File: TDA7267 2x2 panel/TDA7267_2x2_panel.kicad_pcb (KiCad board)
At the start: 2 copper layers, 89 x 81 mm, 72 parts, among them U1 TDA7267

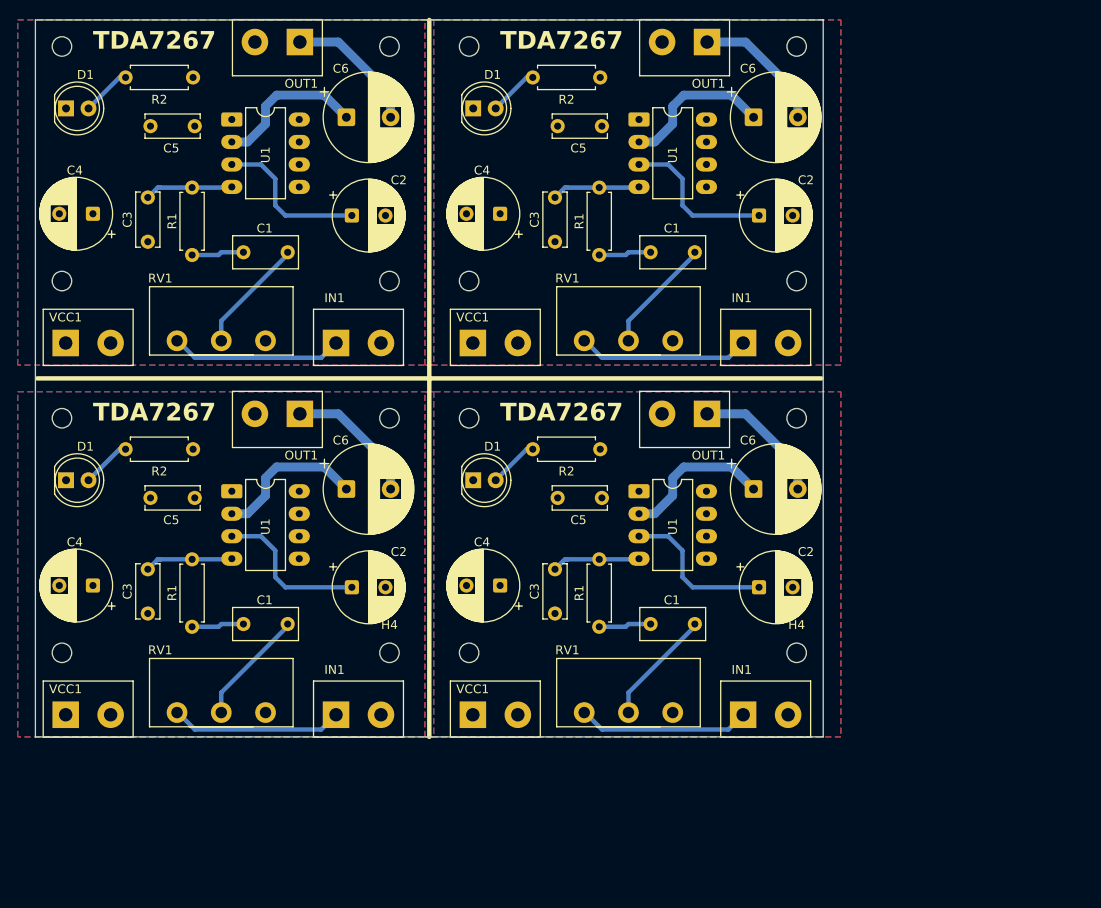
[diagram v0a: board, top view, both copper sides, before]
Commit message: Bottom GND plane
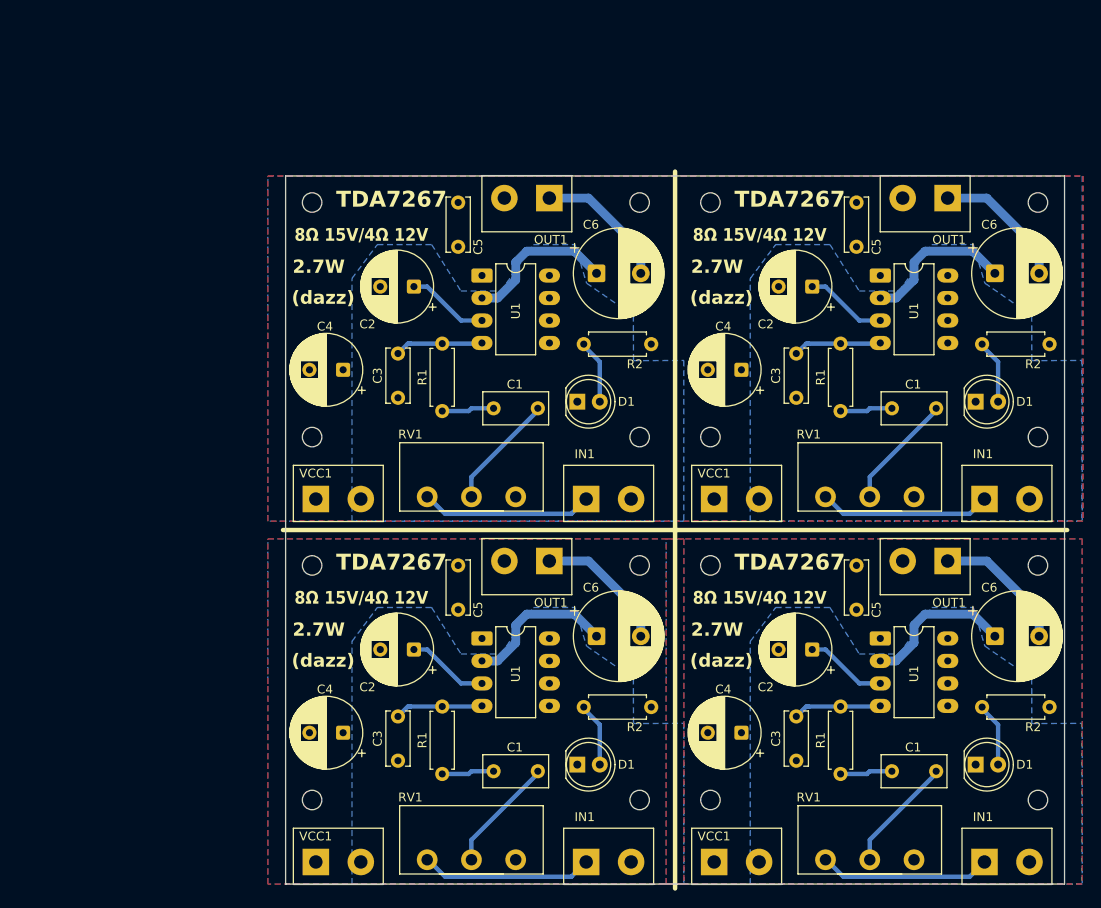
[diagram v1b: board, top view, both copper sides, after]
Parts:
- removed the C1 at (146.5, 97.2)
- removed the C1 at (100.5, 97.2)
- removed the C1 at (100.5, 55.2)
- removed the C1 at (146.5, 55.2)
- removed the C2 at (107.8, 51.1)
- removed the C2 at (153.8, 93.1)
- removed the C2 at (153.8, 51.1)
- removed the C2 at (107.8, 93.1)
- removed the C3 at (130.7, 54.1)
- removed the C3 at (84.7, 96.1)
- removed the C3 at (84.7, 54.1)
- removed the C3 at (130.7, 96.1)
- removed the C4 at (78.5, 92.9)
- removed the C4 at (124.5, 50.9)
- removed the C4 at (78.5, 50.9)
- removed the C4 at (124.5, 92.9)
- removed the C5 at (131.0, 41.0)
- removed the C5 at (131.0, 83.0)
- removed the C5 at (85.0, 41.0)
- removed the C5 at (85.0, 83.0)
- removed the C6 at (107.1, 40.0)
- removed the C6 at (107.1, 82.0)
- removed the C6 at (153.1, 82.0)
- removed the C6 at (153.1, 40.0)
- removed the D1 at (121.5, 39.0)
- removed the D1 at (75.5, 81.0)
- removed the D1 at (75.5, 39.0)
- removed the D1 at (121.5, 81.0)
- removed the H1 at (75.0, 74.0)
- removed the H1 at (75.0, 32.0)
- removed the H1 at (121.0, 32.0)
- removed the H1 at (121.0, 74.0)
- removed the H2 at (158.0, 74.0)
- removed the H2 at (112.0, 32.0)
- removed the H2 at (158.0, 32.0)
- removed the H2 at (112.0, 74.0)
- removed the H3 at (121.0, 100.5)
- removed the H3 at (121.0, 58.5)
- removed the H3 at (75.0, 58.5)
- removed the H3 at (75.0, 100.5)
- removed the H4 at (112.0, 58.5)
- removed the H4 at (158.0, 100.5)
- removed the H4 at (158.0, 58.5)
- removed the H4 at (112.0, 100.5)
- removed the IN1 at (152.0, 107.5)
- removed the IN1 at (106.0, 107.5)
- removed the IN1 at (106.0, 65.5)
- removed the IN1 at (152.0, 65.5)
- removed the OUT1 at (101.9, 73.5)
- removed the OUT1 at (147.9, 73.5)
- removed the OUT1 at (101.9, 31.5)
- removed the OUT1 at (147.9, 31.5)
- removed the R1 at (89.7, 55.6)
- removed the R1 at (135.7, 55.6)
- removed the R1 at (89.7, 97.6)
- removed the R1 at (135.7, 97.6)
- removed the R2 at (128.2, 77.5)
- removed the R2 at (128.2, 35.5)
- removed the R2 at (82.2, 35.5)
- removed the R2 at (82.2, 77.5)
- removed the RV1 at (88.0, 107.2)
- removed the RV1 at (134.0, 65.2)
- removed the RV1 at (134.0, 107.2)
- removed the RV1 at (88.0, 65.2)
- removed the U1 at (94.2, 40.2)
- removed the U1 at (140.2, 40.2)
- removed the U1 at (94.2, 82.2)
- removed the U1 at (140.2, 82.2)
- removed the VCC1 at (75.4, 65.5)
- removed the VCC1 at (121.4, 107.5)
- removed the VCC1 at (75.4, 107.5)
- removed the VCC1 at (121.4, 65.5)
- added C1: 1uF, Capacitor_THT:C_Rect_L7.2mm_W3.5mm_P5.00mm_FKS2_FKP2_MKS2_MKP2, F.Cu at (128.8, 72.9)
- added C1: 1uF, Capacitor_THT:C_Rect_L7.2mm_W3.5mm_P5.00mm_FKS2_FKP2_MKS2_MKP2, F.Cu at (173.8, 113.9)
- added C1: 1uF, Capacitor_THT:C_Rect_L7.2mm_W3.5mm_P5.00mm_FKS2_FKP2_MKS2_MKP2, F.Cu at (173.8, 72.9)
- added C1: 1uF, Capacitor_THT:C_Rect_L7.2mm_W3.5mm_P5.00mm_FKS2_FKP2_MKS2_MKP2, F.Cu at (128.8, 113.9)
- added C2: 47uF, Capacitor_THT:CP_Radial_D8.0mm_P3.80mm, F.Cu at (114.8, 100.1)
- added C2: 47uF, Capacitor_THT:CP_Radial_D8.0mm_P3.80mm, F.Cu at (159.8, 100.1)
- added C2: 47uF, Capacitor_THT:CP_Radial_D8.0mm_P3.80mm, F.Cu at (114.8, 59.1)
- added C2: 47uF, Capacitor_THT:CP_Radial_D8.0mm_P3.80mm, F.Cu at (159.8, 59.1)
- added C3: 470pF, Capacitor_THT:C_Disc_D6.0mm_W2.5mm_P5.00mm, F.Cu at (113.0, 112.7)
- added C3: 470pF, Capacitor_THT:C_Disc_D6.0mm_W2.5mm_P5.00mm, F.Cu at (113.0, 71.7)
- added C3: 470pF, Capacitor_THT:C_Disc_D6.0mm_W2.5mm_P5.00mm, F.Cu at (158.0, 71.7)
- added C3: 470pF, Capacitor_THT:C_Disc_D6.0mm_W2.5mm_P5.00mm, F.Cu at (158.0, 112.7)
- added C4: 100uF, Capacitor_THT:CP_Radial_D8.0mm_P3.80mm, F.Cu at (151.8, 109.5)
- added C4: 100uF, Capacitor_THT:CP_Radial_D8.0mm_P3.80mm, F.Cu at (106.8, 68.5)
- added C4: 100uF, Capacitor_THT:CP_Radial_D8.0mm_P3.80mm, F.Cu at (151.8, 68.5)
- added C4: 100uF, Capacitor_THT:CP_Radial_D8.0mm_P3.80mm, F.Cu at (106.8, 109.5)
- added C5: 100nF, Capacitor_THT:C_Disc_D6.0mm_W2.5mm_P5.00mm, F.Cu at (164.8, 90.6)
- added C5: 100nF, Capacitor_THT:C_Disc_D6.0mm_W2.5mm_P5.00mm, F.Cu at (119.8, 90.6)
- added C5: 100nF, Capacitor_THT:C_Disc_D6.0mm_W2.5mm_P5.00mm, F.Cu at (164.8, 49.6)
- added C5: 100nF, Capacitor_THT:C_Disc_D6.0mm_W2.5mm_P5.00mm, F.Cu at (119.8, 49.6)
- added C6: 1000uF, Capacitor_THT:CP_Radial_D10.0mm_P5.00mm, F.Cu at (180.4, 98.6)
- added C6: 1000uF, Capacitor_THT:CP_Radial_D10.0mm_P5.00mm, F.Cu at (180.4, 57.6)
- added C6: 1000uF, Capacitor_THT:CP_Radial_D10.0mm_P5.00mm, F.Cu at (135.4, 98.6)
- added C6: 1000uF, Capacitor_THT:CP_Radial_D10.0mm_P5.00mm, F.Cu at (135.4, 57.6)
- added D1: LED, LED_THT:LED_D5.0mm, F.Cu at (133.2, 113.1)
- added D1: LED, LED_THT:LED_D5.0mm, F.Cu at (178.2, 72.1)
- added D1: LED, LED_THT:LED_D5.0mm, F.Cu at (133.2, 72.1)
- added D1: LED, LED_THT:LED_D5.0mm, F.Cu at (178.2, 113.1)
- added H1: MountingHole, MountingHole:MountingHole_2.2mm_M2, F.Cu at (148.3, 90.6)
- added H1: MountingHole, MountingHole:MountingHole_2.2mm_M2, F.Cu at (148.3, 49.6)
- added H1: MountingHole, MountingHole:MountingHole_2.2mm_M2, F.Cu at (103.3, 49.6)
- added H1: MountingHole, MountingHole:MountingHole_2.2mm_M2, F.Cu at (103.3, 90.6)
- added H2: MountingHole, MountingHole:MountingHole_2.2mm_M2, F.Cu at (185.3, 49.6)
- added H2: MountingHole, MountingHole:MountingHole_2.2mm_M2, F.Cu at (140.3, 49.6)
- added H2: MountingHole, MountingHole:MountingHole_2.2mm_M2, F.Cu at (140.3, 90.6)
- added H2: MountingHole, MountingHole:MountingHole_2.2mm_M2, F.Cu at (185.3, 90.6)
- added H3: MountingHole, MountingHole:MountingHole_2.2mm_M2, F.Cu at (103.3, 76.1)
- added H3: MountingHole, MountingHole:MountingHole_2.2mm_M2, F.Cu at (148.3, 117.1)
- added H3: MountingHole, MountingHole:MountingHole_2.2mm_M2, F.Cu at (103.3, 117.1)
- added H3: MountingHole, MountingHole:MountingHole_2.2mm_M2, F.Cu at (148.3, 76.1)
- added H4: MountingHole, MountingHole:MountingHole_2.2mm_M2, F.Cu at (140.3, 76.1)
- added H4: MountingHole, MountingHole:MountingHole_2.2mm_M2, F.Cu at (185.3, 117.1)
- added H4: MountingHole, MountingHole:MountingHole_2.2mm_M2, F.Cu at (140.3, 117.1)
- added H4: MountingHole, MountingHole:MountingHole_2.2mm_M2, F.Cu at (185.3, 76.1)
- added IN1: Conn_01x02_Pin, TerminalBlock:TerminalBlock_bornier-2_P5.08mm, F.Cu at (134.2, 124.1)
- added IN1: Conn_01x02_Pin, TerminalBlock:TerminalBlock_bornier-2_P5.08mm, F.Cu at (179.2, 83.1)
- added IN1: Conn_01x02_Pin, TerminalBlock:TerminalBlock_bornier-2_P5.08mm, F.Cu at (134.2, 83.1)
- added IN1: Conn_01x02_Pin, TerminalBlock:TerminalBlock_bornier-2_P5.08mm, F.Cu at (179.2, 124.1)
- added OUT1: Conn_01x02_Pin, TerminalBlock:TerminalBlock_bornier-2_P5.08mm, F.Cu at (130.1, 90.1)
- added OUT1: Conn_01x02_Pin, TerminalBlock:TerminalBlock_bornier-2_P5.08mm, F.Cu at (175.1, 49.1)
- added OUT1: Conn_01x02_Pin, TerminalBlock:TerminalBlock_bornier-2_P5.08mm, F.Cu at (130.1, 49.1)
- added OUT1: Conn_01x02_Pin, TerminalBlock:TerminalBlock_bornier-2_P5.08mm, F.Cu at (175.1, 90.1)
- added R1: 1K, Resistor_THT:R_Axial_DIN0207_L6.3mm_D2.5mm_P7.62mm_Horizontal, F.Cu at (118.0, 73.2)
- added R1: 1K, Resistor_THT:R_Axial_DIN0207_L6.3mm_D2.5mm_P7.62mm_Horizontal, F.Cu at (163.0, 73.2)
- added R1: 1K, Resistor_THT:R_Axial_DIN0207_L6.3mm_D2.5mm_P7.62mm_Horizontal, F.Cu at (118.0, 114.2)
- added R1: 1K, Resistor_THT:R_Axial_DIN0207_L6.3mm_D2.5mm_P7.62mm_Horizontal, F.Cu at (163.0, 114.2)
- added R2: 1K, Resistor_THT:R_Axial_DIN0207_L6.3mm_D2.5mm_P7.62mm_Horizontal, F.Cu at (179.0, 65.6)
- added R2: 1K, Resistor_THT:R_Axial_DIN0207_L6.3mm_D2.5mm_P7.62mm_Horizontal, F.Cu at (179.0, 106.6)
- added R2: 1K, Resistor_THT:R_Axial_DIN0207_L6.3mm_D2.5mm_P7.62mm_Horizontal, F.Cu at (134.0, 65.6)
- added R2: 1K, Resistor_THT:R_Axial_DIN0207_L6.3mm_D2.5mm_P7.62mm_Horizontal, F.Cu at (134.0, 106.6)
- added RV1: A10K, Potentiometer_THT:Potentiometer_Piher_T-16H_Single_Horizontal, F.Cu at (116.3, 82.9)
- added RV1: A10K, Potentiometer_THT:Potentiometer_Piher_T-16H_Single_Horizontal, F.Cu at (161.3, 123.9)
- added RV1: A10K, Potentiometer_THT:Potentiometer_Piher_T-16H_Single_Horizontal, F.Cu at (116.3, 123.9)
- added RV1: A10K, Potentiometer_THT:Potentiometer_Piher_T-16H_Single_Horizontal, F.Cu at (161.3, 82.9)
- added U1: TDA7267, Package_DIP:DIP-8_W7.62mm_LongPads, F.Cu at (167.5, 57.9)
- added U1: TDA7267, Package_DIP:DIP-8_W7.62mm_LongPads, F.Cu at (122.5, 57.9)
- added U1: TDA7267, Package_DIP:DIP-8_W7.62mm_LongPads, F.Cu at (122.5, 98.9)
- added U1: TDA7267, Package_DIP:DIP-8_W7.62mm_LongPads, F.Cu at (167.5, 98.9)
- added VCC1: Conn_01x02_Pin, TerminalBlock:TerminalBlock_bornier-2_P5.08mm, F.Cu at (148.7, 83.1)
- added VCC1: Conn_01x02_Pin, TerminalBlock:TerminalBlock_bornier-2_P5.08mm, F.Cu at (103.7, 83.1)
- added VCC1: Conn_01x02_Pin, TerminalBlock:TerminalBlock_bornier-2_P5.08mm, F.Cu at (148.7, 124.1)
- added VCC1: Conn_01x02_Pin, TerminalBlock:TerminalBlock_bornier-2_P5.08mm, F.Cu at (103.7, 124.1)
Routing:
- net Net-(U1-SRV): track 70.8 -> 37.1 mm
- net Net-(D1-A): track 22.6 -> 29.0 mm
- added copper zone on B.Cu, net /VCC
- added copper zone on B.Cu, net GND
- removed copper zone on B.Cu, net Net-(U1-V+)
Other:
- board size 89 x 81 mm -> 88 x 80 mm
- board text added: "(dazz)"
- board text added: "2.7W"
- board text added: "8Ω 15V/4Ω 12V"
- board text added: "TDA7267 2.7W Amplifier. 5 to 15V DC supply."
- board text removed: "TDA7267 2W Amplifier. 5 to 15V DC supply."

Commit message: Tweaks
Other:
- board text removed: "TDA7267 2.7W Amplifier. 5 to 15V DC supply."
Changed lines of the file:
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@@
 				(thickness 0.035)
 			)
-			(layer "dielectric 1"
+			(layer "dielectric 2"
 				(type "core")
 				(thickness 1.51)
@@
 		)
 	)
-	(gr_text "TDA7267 2.7W Amplifier.\n5 to 15V DC supply."
-		(at 135.261 80.029 0)
-		(layer "B.SilkS")
-		(effects
-			(font
-				(size 1.5 1.5)
-				(thickness 0.3)
-			)
-			(justify left bottom mirror)
-		)
-	)
-	(gr_text "TDA7267 2.7W Amplifier.\n5 to 15V DC supply."
-		(at 180.261 80.029 0)
-		(layer "B.SilkS")
-		(effects
-			(font
-				(size 1.5 1.5)
-				(thickness 0.3)
-			)
-			(justify left bottom mirror)
-		)
-	)
-	(gr_text "TDA7267 2.7W Amplifier.\n5 to 15V DC supply."
-		(at 180.261 121.029 0)
-		(layer "B.SilkS")
-		(effects
-			(font
-				(size 1.5 1.5)
-				(thickness 0.3)
-			)
-			(justify left bottom mirror)
-		)
-	)
-	(gr_text "TDA7267 2.7W Amplifier.\n5 to 15V DC supply."
-		(at 135.261 121.029 0)
-		(layer "B.SilkS")
-		(effects
-			(font
-				(size 1.5 1.5)
-				(thickness 0.3)
-			)
-			(justify left bottom mirror)
-		)
-	)
 	(segment
 		(start 121.261 72.879)
@@
 		(hatch edge 0.5)
 		(connect_pads yes
-			(clearance 0.25)
-		)
-		(min_thickness 0.25)
-		(filled_areas_thickness no)
-		(fill yes
-			(thermal_gap 0.5)
-			(thermal_bridge_width 10)
-		)
-		(polygon
-			(pts
-				(xy 98.261 104.029) (xy 98.261 87.629) (xy 145.261 87.629) (xy 145.261 126.629) (xy 98.261 126.629)
-			)
-		)
-	)
-	(zone
-		(net 3)
-		(net_name "GND")
-		(layer "F.Cu")
-		(hatch edge 0.5)
-		(connect_pads yes
-			(clearance 0.25)
+			(clearance 0.3)
 		)
 		(min_thickness 0.25)
@@
 		(polygon
 			(pts
-				(xy 143.261 104.029) (xy 143.261 87.629) (xy 190.261 87.629) (xy 190.261 126.629) (xy 143.261 126.629)
+				(xy 98.261 104.029) (xy 98.261 87.629) (xy 190.261 87.629) (xy 190.261 126.629) (xy 98.261 126.629)
 			)
 		)
@@
 		(hatch edge 0.5)
 		(connect_pads yes
-			(clearance 0.25)
+			(clearance 0.3)
 		)
 		(min_thickness 0.25)
@@
 		(priority 1)
 		(connect_pads yes
-			(clearance 0.5)
+			(clearance 0.3)
 		)
 		(min_thickness 0.25)
@@
 		(hatch edge 0.5)
 		(connect_pads yes
-			(clearance 0.5)
+			(clearance 0.3)
 		)
 		(min_thickness 0.25)
@@
 		(polygon
 			(pts
-				(xy 98.261 87.629) (xy 145.261 87.629) (xy 145.261 126.629) (xy 98.261 126.629)
+				(xy 98.261 87.629) (xy 190.261 87.629) (xy 190.261 126.629) (xy 98.261 126.629)
 			)
 		)
@@
 		(hatch edge 0.5)
 		(connect_pads yes
-			(clearance 0.5)
+			(clearance 0.3)
 		)
 		(min_thickness 0.25)
@@
 		(priority 1)
 		(connect_pads yes
-			(clearance 0.5)
+			(clearance 0.3)
 		)
 		(min_thickness 0.25)
@@
 		(priority 1)
 		(connect_pads yes
-			(clearance 0.5)
+			(clearance 0.3)
 		)
 		(min_thickness 0.25)
@@
 		(priority 1)
 		(connect_pads yes
-			(clearance 0.5)
+			(clearance 0.3)
 		)
 		(min_thickness 0.25)
@@
 			)
 		)
-	)
-	(zone
-		(net 10)
-		(net_name "/VCC")
-		(layer "B.Cu")
-		(hatch edge 0.5)
-		(connect_pads yes
-			(clearance 0.5)
-		)
-		(min_thickness 0.25)
-		(filled_areas_thickness no)
-		(fill yes
-			(thermal_gap 0.5)
-			(thermal_bridge_width 10)
-		)
-		(polygon
-			(pts
-				(xy 143.261 87.629) (xy 190.261 87.629) (xy 190.261 126.629) (xy 143.261 126.629)
-			)
-		)

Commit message: Tweaks
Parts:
- moved C1 1.26 mm to (127.5, 72.9)
- moved C1 1.26 mm to (172.5, 113.9)
- moved C1 1.26 mm to (172.5, 72.9)
- moved C1 1.26 mm to (127.5, 113.9)
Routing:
- net Net-(C1-Pad2): track 23.7 -> 18.7 mm
- net Net-(C1-Pad1): track 52.4 -> 50.3 mm
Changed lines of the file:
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@@
 		(tags "C Disc series Radial pin pitch 5.00mm diameter 6mm width 2.5mm Capacitor")
 		(property "Reference" "C5"
-			(at 5 -2.25 270)
+			(at 4.871 -2.239 270)
 			(layer "F.SilkS")
 			(effects
@@
 		(tags "C Disc series Radial pin pitch 5.00mm diameter 6mm width 2.5mm Capacitor")
 		(property "Reference" "C5"
-			(at 5 -2.25 270)
+			(at 4.871 -2.25 270)
 			(layer "F.SilkS")
 			(effects
@@
 	(footprint "Capacitor_THT:C_Rect_L7.2mm_W3.5mm_P5.00mm_FKS2_FKP2_MKS2_MKP2"
 		(layer "F.Cu")
-		(at 128.761 72.879 180)
+		(at 127.5 72.879 180)
 		(descr "C, Rect series, Radial, pin pitch=5.00mm, length*width=7.2*3.5mm^2, Capacitor, http://www.wima.com/EN/WIMA_FKS_2.pdf")
 		(tags "C Rect series Radial pin pitch 5.00mm length 7.2mm width 3.5mm Capacitor")
@@
 		(tags "C Disc series Radial pin pitch 5.00mm diameter 6mm width 2.5mm Capacitor")
 		(property "Reference" "C5"
-			(at 5 -2.25 270)
+			(at 4.871 -2.239 270)
 			(layer "F.SilkS")
 			(effects
@@
 		(tags "C Disc series Radial pin pitch 5.00mm diameter 6mm width 2.5mm Capacitor")
 		(property "Reference" "C5"
-			(at 5 -2.25 270)
+			(at 4.871 -2.25 270)
 			(layer "F.SilkS")
 			(effects
@@
 		(tags "Resistor Axial_DIN0207 series Axial Horizontal pin pitch 7.62mm 0.25W = 1/4W length 6.3mm diameter 2.5mm")
 		(property "Reference" "R2"
-			(at 5.7621 2.258863 0)
+			(at 3.799 2.258863 0)
 			(layer "F.SilkS")
 			(effects
@@
 	(footprint "Capacitor_THT:C_Rect_L7.2mm_W3.5mm_P5.00mm_FKS2_FKP2_MKS2_MKP2"
 		(layer "F.Cu")
-		(at 173.761 113.879 180)
+		(at 172.5 113.879 180)
 		(descr "C, Rect series, Radial, pin pitch=5.00mm, length*width=7.2*3.5mm^2, Capacitor, http://www.wima.com/EN/WIMA_FKS_2.pdf")
 		(tags "C Rect series Radial pin pitch 5.00mm length 7.2mm width 3.5mm Capacitor")
@@
 		(tags "Resistor Axial_DIN0207 series Axial Horizontal pin pitch 7.62mm 0.25W = 1/4W length 6.3mm diameter 2.5mm")
 		(property "Reference" "R2"
-			(at 5.7621 2.258863 0)
+			(at 3.799 2.258863 0)
 			(layer "F.SilkS")
 			(effects
@@
 		(tags "Resistor Axial_DIN0207 series Axial Horizontal pin pitch 7.62mm 0.25W = 1/4W length 6.3mm diameter 2.5mm")
 		(property "Reference" "R2"
-			(at 5.7621 2.258863 0)
+			(at 4.049 2.258863 0)
 			(layer "F.SilkS")
 			(effects
@@
 	(footprint "Capacitor_THT:C_Rect_L7.2mm_W3.5mm_P5.00mm_FKS2_FKP2_MKS2_MKP2"
 		(layer "F.Cu")
-		(at 173.761 72.879 180)
+		(at 172.5 72.879 180)
 		(descr "C, Rect series, Radial, pin pitch=5.00mm, length*width=7.2*3.5mm^2, Capacitor, http://www.wima.com/EN/WIMA_FKS_2.pdf")
 		(tags "C Rect series Radial pin pitch 5.00mm length 7.2mm width 3.5mm Capacitor")
@@
 		(tags "Resistor Axial_DIN0207 series Axial Horizontal pin pitch 7.62mm 0.25W = 1/4W length 6.3mm diameter 2.5mm")
 		(property "Reference" "R2"
-			(at 5.7621 2.258863 0)
+			(at 3.885686 2.256117 0)
 			(layer "F.SilkS")
 			(effects
@@
 	(footprint "Capacitor_THT:C_Rect_L7.2mm_W3.5mm_P5.00mm_FKS2_FKP2_MKS2_MKP2"
 		(layer "F.Cu")
-		(at 128.761 113.879 180)
+		(at 127.5 113.879 180)
 		(descr "C, Rect series, Radial, pin pitch=5.00mm, length*width=7.2*3.5mm^2, Capacitor, http://www.wima.com/EN/WIMA_FKS_2.pdf")
 		(tags "C Rect series Radial pin pitch 5.00mm length 7.2mm width 3.5mm Capacitor")
@@
 	)
 	(segment
-		(start 121.261 72.879)
-		(end 123.761 72.879)
+		(start 166.287704 73.215391)
+		(end 162.937704 73.215391)
 		(width 0.5)
 		(layer "B.Cu")
@@
 	)
 	(segment
-		(start 165.951 114.189)
-		(end 166.261 113.879)
+		(start 122.505096 113.87676)
+		(end 121.626096 113.87676)
 		(width 0.5)
 		(layer "B.Cu")
@@
 	)
 	(segment
-		(start 117.961 114.189)
-		(end 120.951 114.189)
+		(start 121.316096 114.18676)
+		(end 117.966096 114.18676)
 		(width 0.5)
 		(layer "B.Cu")
@@
 	)
 	(segment
-		(start 121.261 113.879)
-		(end 123.761 113.879)
+		(start 121.621 72.879)
+		(end 121.311 73.189)
 		(width 0.5)
 		(layer "B.Cu")
@@
 	)
 	(segment
-		(start 120.951 73.189)
-		(end 121.261 72.879)
+		(start 121.311 73.189)
+		(end 117.961 73.189)
 		(width 0.5)
 		(layer "B.Cu")
@@
 	)
 	(segment
-		(start 166.261 72.879)
-		(end 168.761 72.879)
+		(start 166.623762 113.868448)
+		(end 166.313762 114.178448)
 		(width 0.5)
 		(layer "B.Cu")
@@
 	)
 	(segment
-		(start 120.951 114.189)
-		(end 121.261 113.879)
+		(start 167.502762 113.868448)
+		(end 166.623762 113.868448)
 		(width 0.5)
 		(layer "B.Cu")
@@
 	)
 	(segment
-		(start 162.961 114.189)
-		(end 165.951 114.189)
+		(start 121.626096 113.87676)
+		(end 121.316096 114.18676)
 		(width 0.5)
 		(layer "B.Cu")
@@
 	)
 	(segment
-		(start 166.261 113.879)
-		(end 168.761 113.879)
+		(start 166.597704 72.905391)
+		(end 166.287704 73.215391)
 		(width 0.5)
 		(layer "B.Cu")
@@
 	)
 	(segment
-		(start 165.951 73.189)
-		(end 166.261 72.879)
+		(start 122.5 72.879)
+		(end 121.621 72.879)
 		(width 0.5)
 		(layer "B.Cu")
@@
 	)
 	(segment
-		(start 117.961 73.189)
-		(end 120.951 73.189)
+		(start 167.476704 72.905391)
+		(end 166.597704 72.905391)
 		(width 0.5)
 		(layer "B.Cu")
@@
 	)
 	(segment
-		(start 162.961 73.189)
-		(end 165.951 73.189)
+		(start 166.313762 114.178448)
+		(end 162.963762 114.178448)
 		(width 0.5)
 		(layer "B.Cu")
@@
 	)
 	(segment
-		(start 173.761 72.879)
-		(end 173.761 73.129)
+		(start 172.502762 115.989448)
+		(end 172.502762 113.868448)
 		(width 0.5)
 		(layer "B.Cu")
@@
 	)
 	(segment
-		(start 128.761 114.129)
-		(end 121.261 121.629)
+		(start 121.266096 123.87676)
+		(end 121.266096 122.23676)
 		(width 0.5)
 		(layer "B.Cu")
@@
 	)
 	(segment
-		(start 121.261 80.629)
-		(end 121.261 82.879)
+		(start 121.261 81.239)
+		(end 127.5 75)
 		(width 0.5)
 		(layer "B.Cu")
@@
 	)
 	(segment
-		(start 173.761 114.129)
-		(end 166.261 121.629)
+		(start 166.237704 81.265391)
+		(end 172.476704 75.026391)
 		(width 0.5)
 		(layer "B.Cu")
@@
 	)
 	(segment
-		(start 128.761 72.879)
-		(end 128.761 73.129)
+		(start 166.263762 122.228448)
+		(end 172.502762 115.989448)
 		(width 0.5)
 		(layer "B.Cu")
@@
 	)
 	(segment
-		(start 166.261 121.629)
-		(end 166.261 123.879)
+		(start 166.263762 123.868448)
+		(end 166.263762 122.228448)
 		(width 0.5)
 		(layer "B.Cu")
@@
 	)
 	(segment
-		(start 166.261 80.629)
-		(end 166.261 82.879)
+		(start 166.237704 82.905391)
+		(end 166.237704 81.265391)
 		(width 0.5)
 		(layer "B.Cu")
@@
 	)
 	(segment
-		(start 121.261 121.629)
-		(end 121.261 123.879)
+		(start 127.5 75)
+		(end 127.5 72.879)
 		(width 0.5)
 		(layer "B.Cu")
@@
 	)
 	(segment
-		(start 173.761 73.129)
-		(end 166.261 80.629)
+		(start 127.505096 115.99776)
+		(end 127.505096 113.87676)
 		(width 0.5)
 		(layer "B.Cu")
@@
 	)
 	(segment
-		(start 173.761 113.879)
-		(end 173.761 114.129)
+		(start 121.266096 122.23676)
+		(end 127.505096 115.99776)
 		(width 0.5)
 		(layer "B.Cu")
@@
 	)
 	(segment
-		(start 128.761 113.879)
-		(end 128.761 114.129)
+		(start 172.476704 75.026391)
+		(end 172.476704 72.905391)
 		(width 0.5)
 		(layer "B.Cu")
@@
 	)
 	(segment
-		(start 128.761 73.129)
-		(end 121.261 80.629)
+		(start 121.261 82.879)
+		(end 121.261 81.239)
 		(width 0.5)
 		(layer "B.Cu")
